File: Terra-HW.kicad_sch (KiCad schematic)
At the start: 3 parts

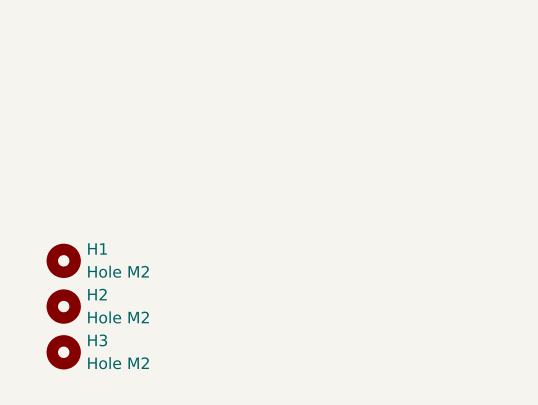
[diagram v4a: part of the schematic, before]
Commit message: Component placement for -004 board outline.
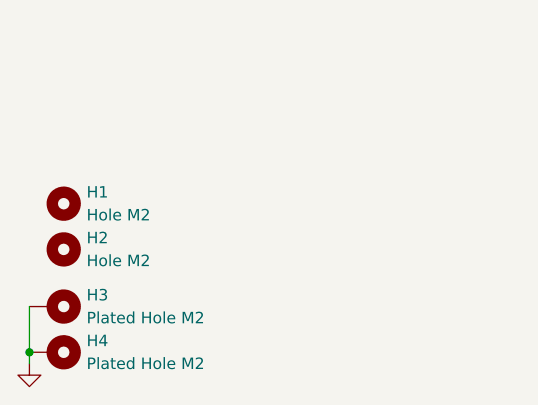
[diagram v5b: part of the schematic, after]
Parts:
- removed H3: Hole M2, MountingHole:MountingHole_2.2mm_M2, symbol Mechanical:MountingHole
- added H3, H4: Plated Hole M2, MountingHole:MountingHole_2.2mm_M2_Pad, symbol Mechanical:MountingHole_Pad
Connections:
- new net GND: H3.1, H4.1
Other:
- moved on the sheet: H1, H2
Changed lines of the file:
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@@
 		)
+	)
+	(junction
+		(at 15.24 191.77)
+		(diameter 0)
+		(color 0 0 0 0)
 	)
 	(wire
@@
 	(wire
 		(pts
+			(xy 15.24 191.77) (xy 15.24 193.04)
+		)
+		(stroke
+			(width 0)
+			(type default)
+		)
+	)
+	(wire
+		(pts
 			(xy 137.16 128.27) (xy 152.4 128.27)
 		)
@@
 		(pts
 			(xy 137.16 111.76) (xy 152.4 111.76)
+		)
+		(stroke
+			(width 0)
+			(type default)
+		)
+	)
+	(wire
+		(pts
+			(xy 15.24 186.69) (xy 15.24 191.77)
 		)
 		(stroke
@@
 			"AAAAAAAAAAAAAAAAAAAAAAAAAAAAAAAAAAAAAAAAAAAAAAAAAAAAAAAAAAAAAAAAAAAAAAAAAAAA"
 			"AAAAAAAAAAAAAAAAAAAAAAAAAAAAAAAAAAAAAAAAAAAAAAAAAAAAAAAAAAAAAAAAAAAAAAAAAAAA"
+			"AAAAAAAAAAAAAAAAAAAAAAAAAAAAAAAAAAAAAAAAAAAAAAAAAAAAAAAAAAAAAAAAAAAAAAAAAAAA"
+			"AAAAAAAAAAAAAADSQiUAAQAAAAAAAAAAAAAAAAAAAAAAAAAAAAAAAAAAAAAAAAAAAAAAUPgMAAEA"
+			"AAAAAAAAAAAAAAAAAAAAAAAAAAAAAAAAAAAAAAAAAAAAAI+oUgABAAAAAAAAAAAAAAAAAAAAAAAA"
+			"AAAAAAAAAAAAAAAAAAAAAABwolEAAQAAAAAAAAAAAAAAAAAAAAAAAAAAAAAAAAAAAAAAAAAAAAAA"
+			"UPgMAAEAAAAAAAAAAAAAAAAAAAAAAAAAAAAAAAAAAAAAAAAAAAAAAFqjUQABAAAAAAAAAAAAAAAA"
+			"AAAAAAAAAAAAAAAAAAAAAAAAAAAAAADKilIAAQAAAAAAAAAAAAAAAAAAAAAAAAAAAAAAAAAAAAAA"
+			"AAAAAAAAwQAzAAEAAAAAAAAAAAAAAAAAAAAAAAAAAAAAAAAAAAAAAAAAAAAAAOUiYQABAAAAAAAA"
+			"AAAAAAAAAAAAAAAAAAAAAAAAAAAAAAAAAAAAAACfw1oAAQAAAAAAAAAAAAAAAAAAAAAAAAAAAAAA"
+			"AAAAAAAAAAAAAAAAUPgMAAEAAAAAAAAAAAAAAAAAAAAAAAAAAAAAAAAAAAAAAAAAAAAAABXIUgAB"
+			"AAAAAAAAAAAAAAAAAAAAAAAAAAAAAAAAAAAAAAAAAAAAAABao1EAAQAAAAAAAAAAAAAAAAAAAAAA"
+			"AAAAAAAAAAAAAAAAAAAAAAAAUPgMAAEAAAAAAAAAAAAAAAAAAAAAAAAAAAAAAAAAAAAAAAAAAAAA"
+			"AA/kVQABNcAAAAAAAAAAAAAAAAAAAAAAAAAAAAAAAAAAAAAAAAAAAAAVyFIAAQAAAAAAAAAAAAAA"
+			"AAAAAAAAAAAAAAAAAAAAAAAAAAAAAAAAL2RmAAE1wAAAAAAAAAAAAAAAAAAAAAAAAAAAAAAAAAAA"
+			"AAAAAAAAAFKhQwABAAAAAAAAAAAAAAAAAAAAAAAAAAAAAAAAAAAAAAAAAAAAAACPkEgAAQAAAAAA"
+			"AAAAAAAAAAAAAAAAAAAAAAAAAAAAAAAAAAAAAAAAeObBAAEAAAAAAAAAAAAAAAAAAAAAAAAAAAAA"
+			"AAAAAAAAAAAAAAAAAC9kZgABAAAAAAAAAAAAAAAAAAAAAAAAAAAAAAAAAAAAAAAAAAAAAACHtFwA"
+			"AQAAAAAAAAAAAAAAAAAAAAAAAAAAAAAAAAAAAAAAAAAAAAAAUPgMAAEAAAAAAAAAAAAAAAAAAAAA"
+			"AAAAAAAAAAAAAAAJAAAJDjXAACAYRqZGAgAAkF7K6UYCAAAAAAAAAAAAAAAAAAAAAAAAAAAAAAAA"
 			"AAAAAAAAAAAAAAAAAAAAAAAAAAAAAAAAAAAAAAAAAAAAAAAAAA=="
 		)
@@
 	(symbol
 		(lib_id "Mechanical:MountingHole")
-		(at 19.05 181.61 0)
+		(at 19.05 175.26 0)
 		(unit 1)
 		(exclude_from_sim no)
@@
 		(fields_autoplaced yes)
 		(property "Reference" "H1"
-			(at 21.59 180.3399 0)
+			(at 21.59 173.9899 0)
 			(effects
 				(font
@@
 		)
 		(property "Value" "Hole M2"
-			(at 21.59 182.8799 0)
+			(at 21.59 176.5299 0)
 			(effects
 				(font
@@
 		)
 		(property "Footprint" "MountingHole:MountingHole_2.2mm_M2"
-			(at 19.05 181.61 0)
+			(at 19.05 175.26 0)
 			(effects
 				(font
@@
 		)
 		(property "Datasheet" "~"
-			(at 19.05 181.61 0)
+			(at 19.05 175.26 0)
 			(effects
 				(font
@@
 		)
 		(property "Description" "Mounting Hole without connection"
-			(at 19.05 181.61 0)
+			(at 19.05 175.26 0)
 			(effects
 				(font
@@
 	)
 	(symbol
+		(lib_id "Mechanical:MountingHole_Pad")
+		(at 17.78 191.77 270)
+		(unit 1)
+		(exclude_from_sim no)
+		(in_bom no)
+		(on_board yes)
+		(dnp no)
+		(property "Reference" "H4"
+			(at 21.59 190.5 90)
+			(effects
+				(font
+					(size 1.27 1.27)
+				)
+				(justify left)
+			)
+		)
+		(property "Value" "Plated Hole M2"
+			(at 21.59 193.04 90)
+			(effects
+				(font
+					(size 1.27 1.27)
+				)
+				(justify left)
+			)
+		)
+		(property "Footprint" "MountingHole:MountingHole_2.2mm_M2_Pad"
+			(at 17.78 191.77 0)
+			(effects
+				(font
+					(size 1.27 1.27)
+				)
+				(hide yes)
+			)
+		)
+		(property "Datasheet" "~"
+			(at 17.78 191.77 0)
+			(effects
+				(font
+					(size 1.27 1.27)
+				)
+				(hide yes)
+			)
+		)
+		(property "Description" "Mounting Hole with connection"
+			(at 17.78 191.77 0)
+			(effects
+				(font
+					(size 1.27 1.27)
+				)
+				(hide yes)
+			)
+		)
+		(pin "1"
+		)
+		(instances
+			(project "Terra-HW"
+				(path "/acca4a2f-1cc7-44b0-a26a-921257f6c268"
+					(reference "H4")
+					(unit 1)
+				)
+			)
+		)
+	)
+	(symbol
 		(lib_id "Mechanical:MountingHole")
-		(at 19.05 186.69 0)
+		(at 19.05 180.34 0)
 		(unit 1)
 		(exclude_from_sim no)
@@
 		(fields_autoplaced yes)
 		(property "Reference" "H2"
-			(at 21.59 185.4199 0)
+			(at 21.59 179.0699 0)
 			(effects
 				(font
@@
 		)
 		(property "Value" "Hole M2"
-			(at 21.59 187.9599 0)
+			(at 21.59 181.6099 0)
 			(effects
 				(font
@@
 		)
 		(property "Footprint" "MountingHole:MountingHole_2.2mm_M2"
-			(at 19.05 186.69 0)
+			(at 19.05 180.34 0)
 			(effects
 				(font
@@
 		)
 		(property "Datasheet" "~"
-			(at 19.05 186.69 0)
+			(at 19.05 180.34 0)
 			(effects
 				(font
@@
 		)
 		(property "Description" "Mounting Hole without connection"
-			(at 19.05 186.69 0)
+			(at 19.05 180.34 0)
 			(effects
 				(font
@@
 	)
 	(symbol
-		(lib_id "Mechanical:MountingHole")
-		(at 19.05 191.77 0)
+		(lib_id "power:GND")
+		(at 15.24 193.04 0)
+		(unit 1)
+		(exclude_from_sim no)
+		(in_bom yes)
+		(on_board yes)
+		(dnp no)
+		(fields_autoplaced yes)
+		(property "Reference" "#PWR074"
+			(at 15.24 199.39 0)
+			(effects
+				(font
+					(size 1.27 1.27)
+				)
+				(hide yes)
+			)
+		)
+		(property "Value" "GND"
+			(at 15.24 198.12 0)
+			(effects
+				(font
+					(size 1.27 1.27)
+				)
+				(hide yes)
+			)
+		)
+		(property "Footprint" ""
+			(at 15.24 193.04 0)
+			(effects
+				(font
+					(size 1.27 1.27)
+				)
+				(hide yes)
+			)
+		)
+		(property "Datasheet" ""
+			(at 15.24 193.04 0)
+			(effects
+				(font
+					(size 1.27 1.27)
+				)
+				(hide yes)
+			)
+		)
+		(property "Description" "Power symbol creates a global label with name \"GND\" , ground"
+			(at 15.24 193.04 0)
+			(effects
+				(font
+					(size 1.27 1.27)
+				)
+				(hide yes)
+			)
+		)
+		(pin "1"
+		)
+		(instances
+			(project "Terra-HW"
+				(path "/acca4a2f-1cc7-44b0-a26a-921257f6c268"
+					(reference "#PWR074")
+					(unit 1)
+				)
+			)
+		)
+	)
+	(symbol
+		(lib_id "Mechanical:MountingHole_Pad")
+		(at 17.78 186.69 270)
 		(unit 1)
 		(exclude_from_sim no)
@@
 		(on_board yes)
 		(dnp no)
-		(fields_autoplaced yes)
 		(property "Reference" "H3"
-			(at 21.59 190.4999 0)
+			(at 21.59 185.42 90)
 			(effects
 				(font
@@
 			)
 		)
-		(property "Value" "Hole M2"
-			(at 21.59 193.0399 0)
+		(property "Value" "Plated Hole M2"
+			(at 21.59 187.96 90)
 			(effects
 				(font
@@
 			)
 		)
-		(property "Footprint" "MountingHole:MountingHole_2.2mm_M2"
-			(at 19.05 191.77 0)
+		(property "Footprint" "MountingHole:MountingHole_2.2mm_M2_Pad"
+			(at 17.78 186.69 0)
 			(effects
 				(font
@@
 		)
 		(property "Datasheet" "~"
-			(at 19.05 191.77 0)
-			(effects
-				(font
-					(size 1.27 1.27)
-				)
-				(hide yes)
-			)
-		)
-		(property "Description" "Mounting Hole without connection"
-			(at 19.05 191.77 0)
-			(effects
-				(font
-					(size 1.27 1.27)
-				)
-				(hide yes)
-			)
+			(at 17.78 186.69 0)
+			(effects
+				(font
+					(size 1.27 1.27)
+				)
+				(hide yes)
+			)
+		)
+		(property "Description" "Mounting Hole with connection"
+			(at 17.78 186.69 0)
+			(effects
+				(font
+					(size 1.27 1.27)
+				)
+				(hide yes)
+			)
+		)
+		(pin "1"
 		)
 		(instances
-			(project "Terra-HW"
+			(project ""
 				(path "/acca4a2f-1cc7-44b0-a26a-921257f6c268"
 					(reference "H3")

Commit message: Lots of board layout
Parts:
- added FID1, FID2, FID3: Fiducial, Fiducial:Fiducial_1mm_Mask2mm, symbol Mechanical:Fiducial
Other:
- sheet Microcontroller ports: added DISP_DC, DISP_PWM_BL, DISP_~{RST}, SPI_MOSI, SPI_SCK, SPI_~{CS0_DISP}; removed none
- sheet Peripehrals ports: added DISP_DC, DISP_PWM_BL, DISP_~{RST}, SPI_MOSI, SPI_SCK, SPI_~{CS0_DISP}; removed none
- note added: "DISPLAY"
- note added: "GPS"
- note added: "GPS UART"
- note added: "HAPTICS"
- note added: "IMU"
- note added: "IMU/COMPASS HAPTICS"
- moved on the sheet: H1, H2, H3, H4
